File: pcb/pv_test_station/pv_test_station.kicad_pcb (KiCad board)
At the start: 2 copper layers, 16 parts, among them IC1 CT426-HSN830DR, J1 Connector_Panel, J2 Connector_load, J3 Conncector 5V, J4 qwiic, J5 i2c, J6 GPS, K1 AZ576-1A-12DE, Q1 2N7002

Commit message: finished pcb
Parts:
- removed the J3 at (133.4, 99.0)
- added J10: Bat in, Connector_PinHeader_2.54mm:PinHeader_1x02_P2.54mm_Vertical, F.Cu at (74.5, 116.8)
- added J2: Out, digikey-footprints:PHOENIX_1017521, F.Cu at (170.1, 148.0)
- added J4: FRAM, Connector_PinSocket_2.54mm:PinSocket_1x08_P2.54mm_Vertical, F.Cu at (94.5, 57.9)
- added J7: Temp2, Connector_PinHeader_2.54mm:PinHeader_1x04_P2.54mm_Vertical, F.Cu at (77.9, 74.5)
- added U1: ~, digikey-footprints:DCDC, F.Cu at (92.5, 116.8)
- C1: footprint Capacitor_SMD:C_0201_0603Metric -> Capacitor_SMD:C_0603_1608Metric
- D1: footprint Resistor_THT:R_Axial_DIN0204_L3.6mm_D1.6mm_P7.62mm_Horizontal -> digikey-footprints:DIODE_BAR6303WE6327HTSA1_INF
- J1: value Connector_Panel -> In; footprint Connector_Phoenix_MSTB:PhoenixContact_MSTBA_2,5_4-G-5,08_1x04_P5.08mm_Horizontal -> digikey-footprints:PHOENIX_1017521
- J3: renamed from J2; value Connector_load -> load; footprint Connector_Phoenix_MSTB:PhoenixContact_MSTBA_2,5_2-G-5,08_1x02_P5.08mm_Horizontal -> digikey-footprints:PHOENIX_1017521
- J6: renamed from J5; value i2c -> Temp1
- J9: renamed from J6; footprint Connector_PinHeader_2.54mm:PinHeader_1x05_P2.54mm_Vertical -> Connector_PinSocket_2.54mm:PinSocket_1x05_P2.54mm_Vertical
- R1, R2: footprint Resistor_SMD:R_0201_0603Metric -> Resistor_SMD:R_0603_1608Metric
- moved F1 90.3 mm to (103.4, 141.8)
- moved J3 72.4 mm to (170.0, 123.0), turned to 90 degrees
- moved J1 70.9 mm to (70.9, 134.7), turned to -90 degrees
- moved J5 66.7 mm to (74.0, 59.5), turned to -90 degrees
- moved F2 61.0 mm to (126.5, 118.9), turned to 90 degrees
- moved D1 55.1 mm to (135.2, 103.5), turned to 90 degrees
- moved R1 53.5 mm to (136.2, 147.5), turned to 180 degrees
- moved J9 52.2 mm to (94.5, 97.5), turned to 180 degrees
- moved J6 51.9 mm to (77.9, 68.5), turned to 90 degrees
- moved R2 50.1 mm to (131.8, 147.5), turned to 180 degrees
- moved A1 47.8 mm to (123.3, 75.9), turned to 90 degrees
- moved K1 43.5 mm to (142.3, 104.8)
- moved IC1 43.1 mm to (138.1, 130.5), turned to 90 degrees
- moved C1 37.6 mm to (138.2, 125.5), turned to 180 degrees
- moved Q1 30.4 mm to (135.2, 98.5)
- renumbered J4 to J5
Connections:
- net /Relais renamed relais
- A1 pad 2: Net-(A1-3V3) -> +3.3V
- C1 pad 2: Net-(A1-3V3) -> +3.3V
- IC1 pad 8: Net-(A1-3V3) -> +3.3V
- J1 pad 1: /- In -> /+ In
- J1 pad 2: /- In -> GND
- R2 pad 2: /- In -> GND
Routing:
- net +3.3V: track 0.00 -> 206.4 mm
- net /RelaisPin: track 0.00 -> 114.8 mm
- net +5V: track 0.00 -> 112.2 mm, vias 0 -> 2
- net /SDA: track 0.00 -> 107.3 mm
- net /SCL: track 0.00 -> 97.3 mm
- net /V_meter: track 0.00 -> 75.1 mm, vias 0 -> 1
- net /RX: track 0.00 -> 71.9 mm
- net /TX: track 0.00 -> 67.6 mm
- net /PPS: track 0.00 -> 60.2 mm, vias 0 -> 1
- net /A_meter: track 0.00 -> 52.3 mm, vias 0 -> 1
- net /+ Out: track 0.00 -> 16.2 mm
- net Net-(D1-A): track 0.00 -> 15.8 mm
- net GND: track 0.00 -> 14.6 mm, vias 0 -> 5
- net Net-(J10-Pin_1): track 0.00 -> 9.06 mm
- net Net-(J10-Pin_2): track 0.00 -> 8.24 mm
- added copper zone on F.Cu, net /+ In
- added copper zone on F.Cu, net /+ Out
- added copper zone on B.Cu, net GND
- added copper zone on F.Cu, net Net-(IC1-IP+_1)
- added copper zone on F.Cu, net Net-(J3-Pin_2)
- added copper zone on F.Cu, net Net-(K1-COM_1)
- added copper zone on F.Cu, net relais
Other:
- board outline added: 100 x 100 mm

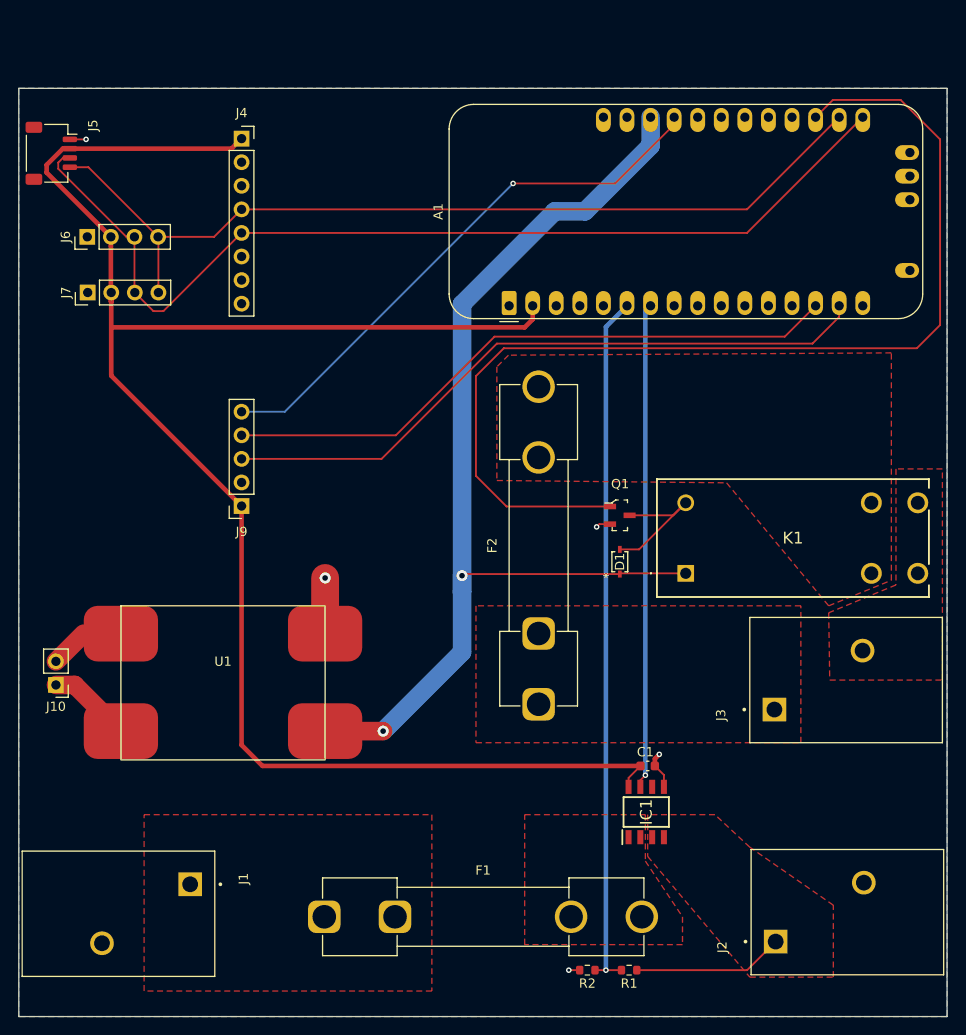
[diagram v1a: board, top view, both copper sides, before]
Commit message: fixed some PCB issues (resistor size, GND on top layer)
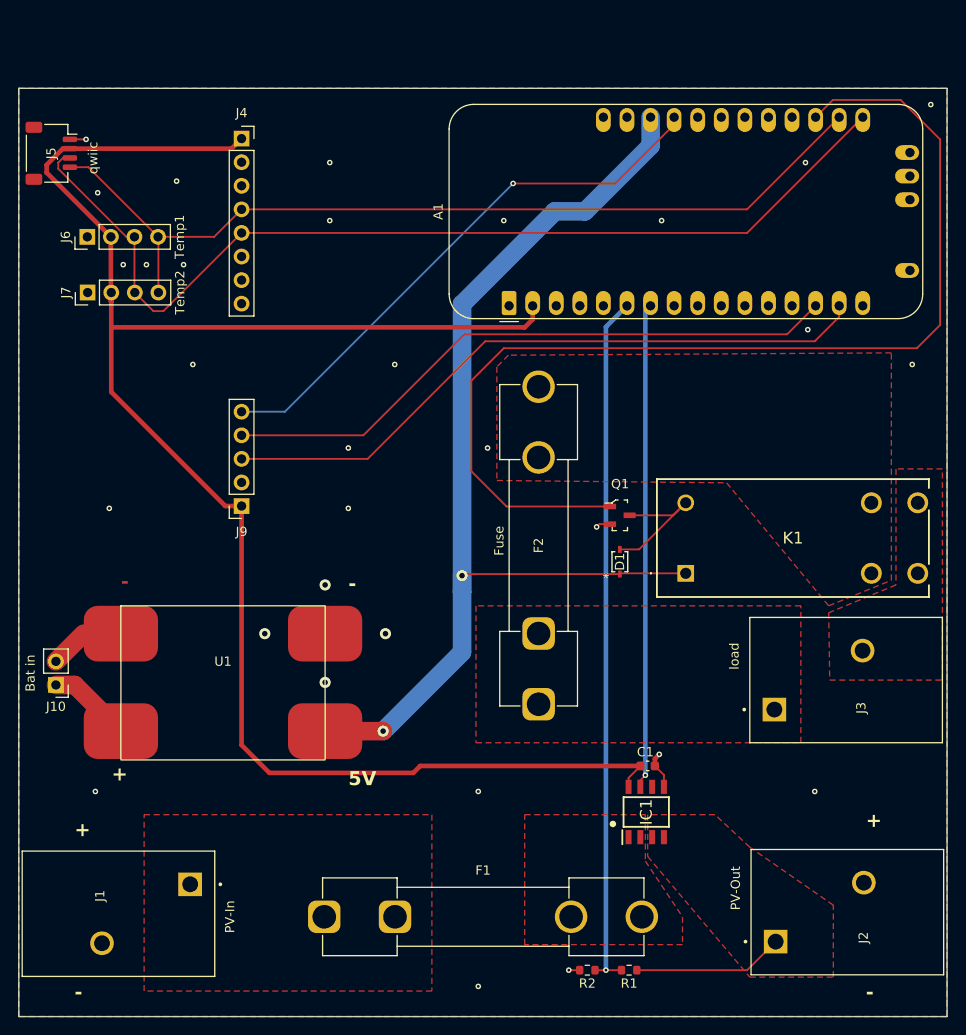
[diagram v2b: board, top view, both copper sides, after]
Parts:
- J1: value In -> PV-In
- J2: value Out -> PV-Out
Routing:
- net GND: track 14.6 -> 8.60 mm, vias 5 -> 31
- net +3.3V: track 206.4 -> 208.1 mm
- added copper zone on F.Cu, net GND
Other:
- board text added: "+"
- board text added: "-"
- board text added: "5V"

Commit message: added docker for db
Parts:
- added R3: nc, Resistor_SMD:R_0603_1608Metric, F.Cu at (100.2, 70.8)
- added R4: nc, Resistor_SMD:R_0603_1608Metric, F.Cu at (100.2, 73.2)
- added R5: nc, Resistor_SMD:R_0603_1608Metric, F.Cu at (100.2, 75.8)
- J6, J7: footprint Connector_PinHeader_2.54mm:PinHeader_1x04_P2.54mm_Vertical -> Connector_PinSocket_2.54mm:PinSocket_1x04_P2.54mm_Vertical
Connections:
- A1 pad 21: unconnected-(A1-D9-Pad21) -> /WP
- J4 pad 3: unconnected-(J4-Pin_3-Pad3) -> /WP
- J4 pad 6: unconnected-(J4-Pin_6-Pad6) -> Net-(J4-Pin_6)
- J4 pad 7: unconnected-(J4-Pin_7-Pad7) -> Net-(J4-Pin_7)
- J4 pad 8: unconnected-(J4-Pin_8-Pad8) -> Net-(J4-Pin_8)
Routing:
- net /WP: track 0.00 -> 60.9 mm
- net +3.3V: track 208.1 -> 232.8 mm
- net Net-(J4-Pin_8): track 0.00 -> 4.95 mm
- net Net-(J4-Pin_6): track 0.00 -> 4.90 mm
- net Net-(J4-Pin_7): track 0.00 -> 4.89 mm
- net GND: vias 31 -> 39
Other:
- outline, holes or cut-outs redrawn
- board text added: "pull up"
